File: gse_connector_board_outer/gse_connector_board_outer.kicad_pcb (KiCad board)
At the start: 2 copper layers, 52 x 27 mm, 9 parts, among them J1 arming_connector, J2 gse_com_connector, J3 chg_connector, J5 Conn_02x02_Top_Bottom, J6 Conn_02x02_Top_Bottom, J7 Conn_02x02_Top_Bottom

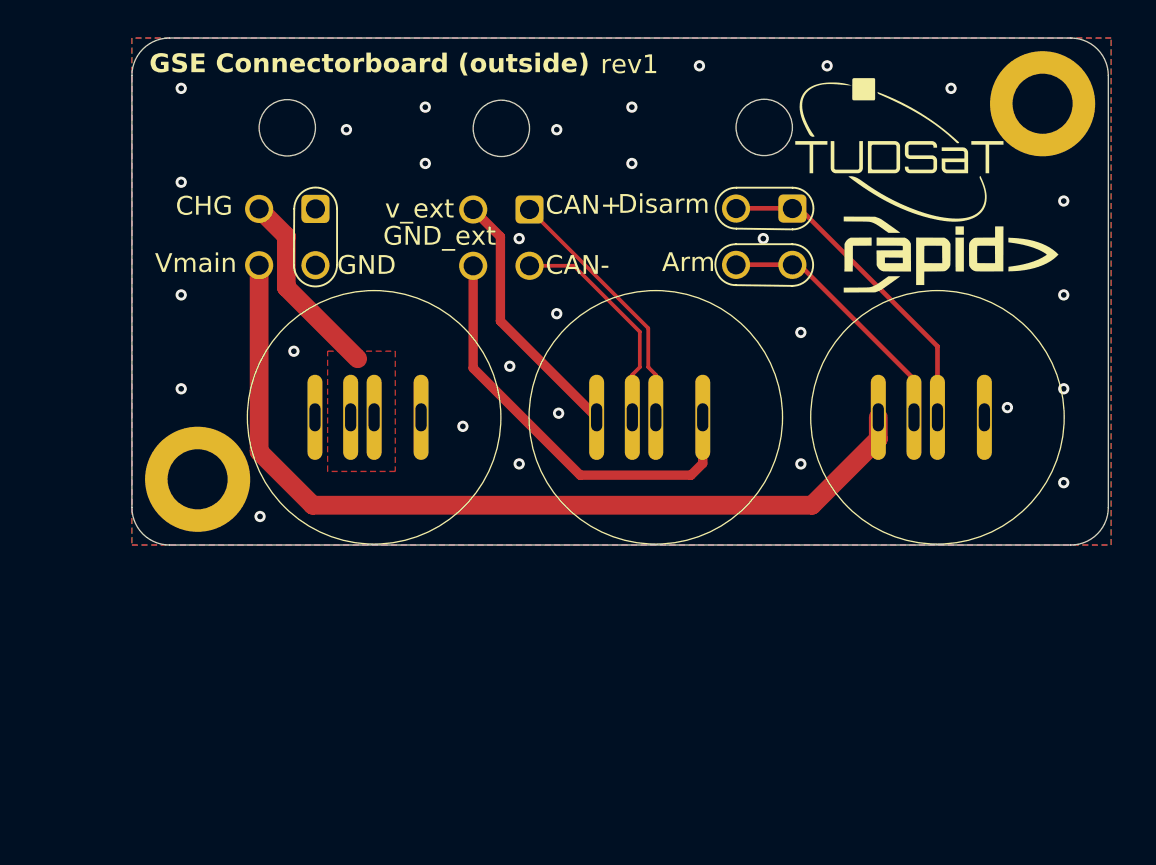
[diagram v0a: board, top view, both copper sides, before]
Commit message: changed the footprints of the magnetic connector and routing of inner board
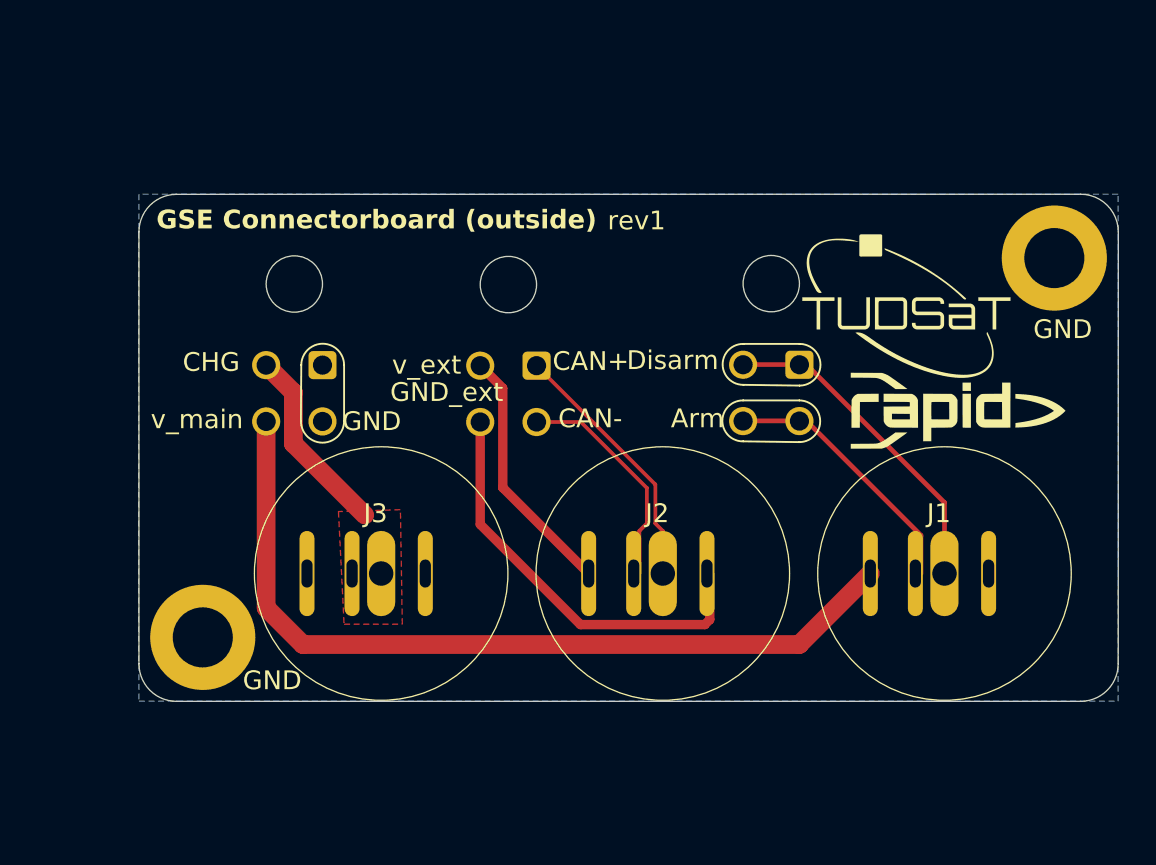
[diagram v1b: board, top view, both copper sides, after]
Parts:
- J1, J2, J3: footprint custom_parts:4_pin_mag_con_new -> custom_parts:4_pin_mag_con_high
- moved H1 8.42 mm to (113.8, 104.9)
- moved J5 8.33 mm to (145.6, 90.4)
- moved J6 8.33 mm to (131.6, 90.5)
- moved J7 8.33 mm to (120.2, 90.4)
- moved G*** 8.33 mm to (154.0, 92.8)
- moved J1 8.33 mm to (153.3, 104.5)
- moved J2 8.33 mm to (138.3, 104.5)
- moved J3 8.33 mm to (123.3, 104.5)
- moved H2 8.24 mm to (159.1, 84.7)
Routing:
- net main_voltage: track 46.7 -> 44.5 mm
- net GND: vias 29 -> 0
- removed copper zone on F.Cu, net GND
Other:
- board size 52 x 27 mm -> 52.2 x 27 mm
- board text added: "v_main"
- board text removed: "JLCJLCJLC"
- board text removed: "Vmain"

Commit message: adapted footprints, scematics and routing
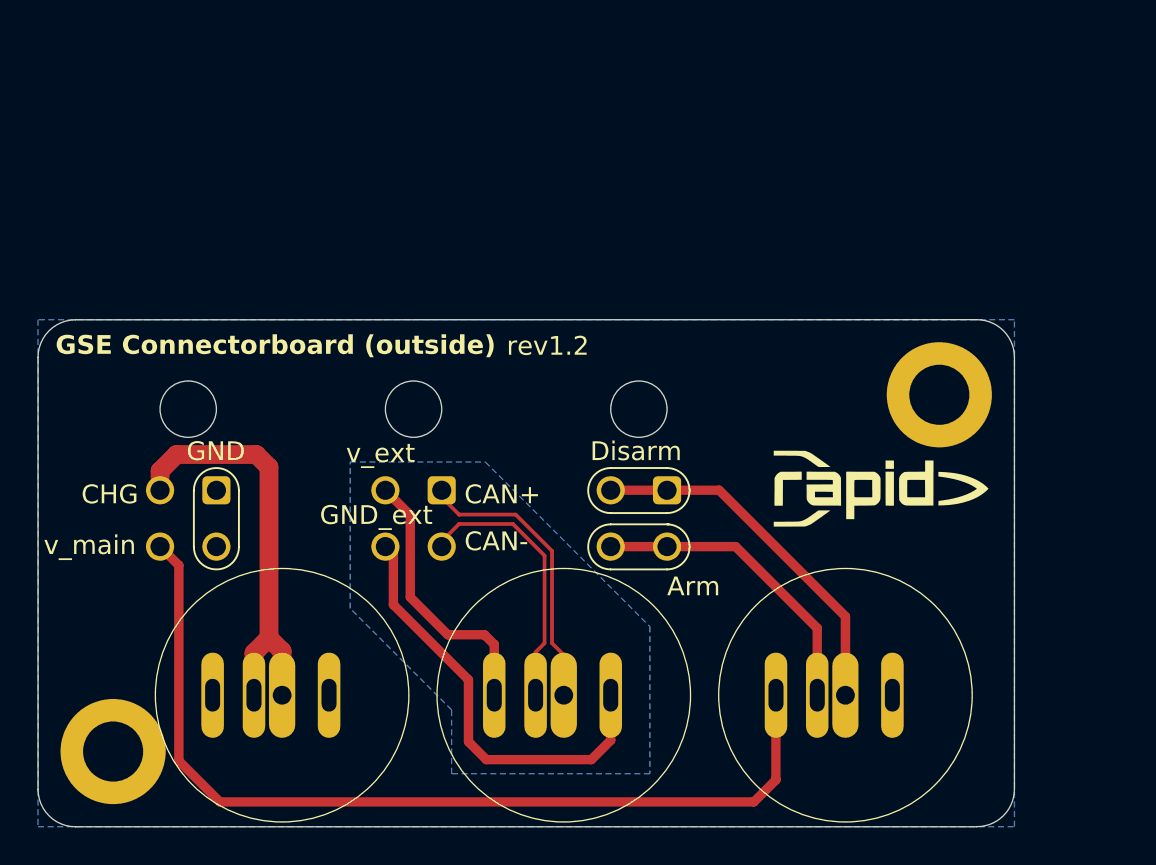
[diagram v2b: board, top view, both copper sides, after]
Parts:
- moved J5 9.72 mm to (138.5, 97.1)
- moved H2 9.51 mm to (153.0, 92.0)
- moved J7 8.74 mm to (114.5, 97.1)
- moved J1 8.36 mm to (148.0, 111.0)
- moved J2 8.36 mm to (133.0, 111.0)
- moved J3 8.36 mm to (118.0, 111.0)
- moved J6 8.34 mm to (126.5, 97.1)
- moved H1 7.73 mm to (109.0, 111.0)
- moved G*** 5.83 mm to (149.9, 97.0)
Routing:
- net CHG: track 10.2 -> 23.3 mm
- net main_voltage: track 44.5 -> 49.5 mm
- net arm: track 13.7 -> 18.4 mm
- net disarm: track 17.2 -> 19.5 mm
- net CAN_ext+: track 12.7 -> 14.7 mm
- net CAN_ext-: track 13.9 -> 15.6 mm
- net +V_EXT: track 13.5 -> 14.5 mm
- net GND_EXT: track 22.5 -> 23.0 mm
- added copper zone on B.Cu, net GND_EXT
- removed copper zone on F.Cu, net CHG
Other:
- board size 52.2 x 27 mm -> 52 x 27 mm
- board text added: "rev1.2"
- board text removed: "rev1"

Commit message: implemented changes
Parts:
- J1, J2, J3: footprint custom_parts:4_pin_mag_con_high -> custom_parts:4_pin_mag_con_new
- moved G*** 8.16 mm to (144.6, 90.8)
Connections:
- J1 pad 1: main_voltage -> Voltage_Arm
- J1 pad 4: GND -> GND_Arm
- J5 pad 1: disarm -> GND_Arm
- J5 pad 3: arm -> Voltage_Arm
- J7 pad 2: CHG -> GND
- J7 pad 3: GND -> CHG
- J7 pad 4: main_voltage -> CHG
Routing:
- net main_voltage: track 49.5 -> 0.00 mm
- net Voltage_Arm: track 0.00 -> 27.4 mm
- net CHG: track 23.3 -> 15.7 mm
- net CAN_ext-: track 15.6 -> 12.9 mm
- net disarm: track 19.5 -> 21.0 mm
- net arm: track 18.4 -> 17.5 mm
- added copper zone on B.Cu, net GND_Arm
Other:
- board text added: "+"
- board text added: "-"
- board text added: "CAN"
- board text added: "arm"
- board text added: "d.arm"
- board text added: "gnd_arm"
- board text added: "rev1"
- board text added: "v_CHG"
- board text added: "v_arm"
- board text removed: "rev1.2"
